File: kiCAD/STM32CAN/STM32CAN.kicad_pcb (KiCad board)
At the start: 2 copper layers, 10.2 x 20.3 mm, 6 parts, among them IC1 STM32F042G6U6, IC2 TCAN332GDCNR, Y1 7A-8.000MAAE-T

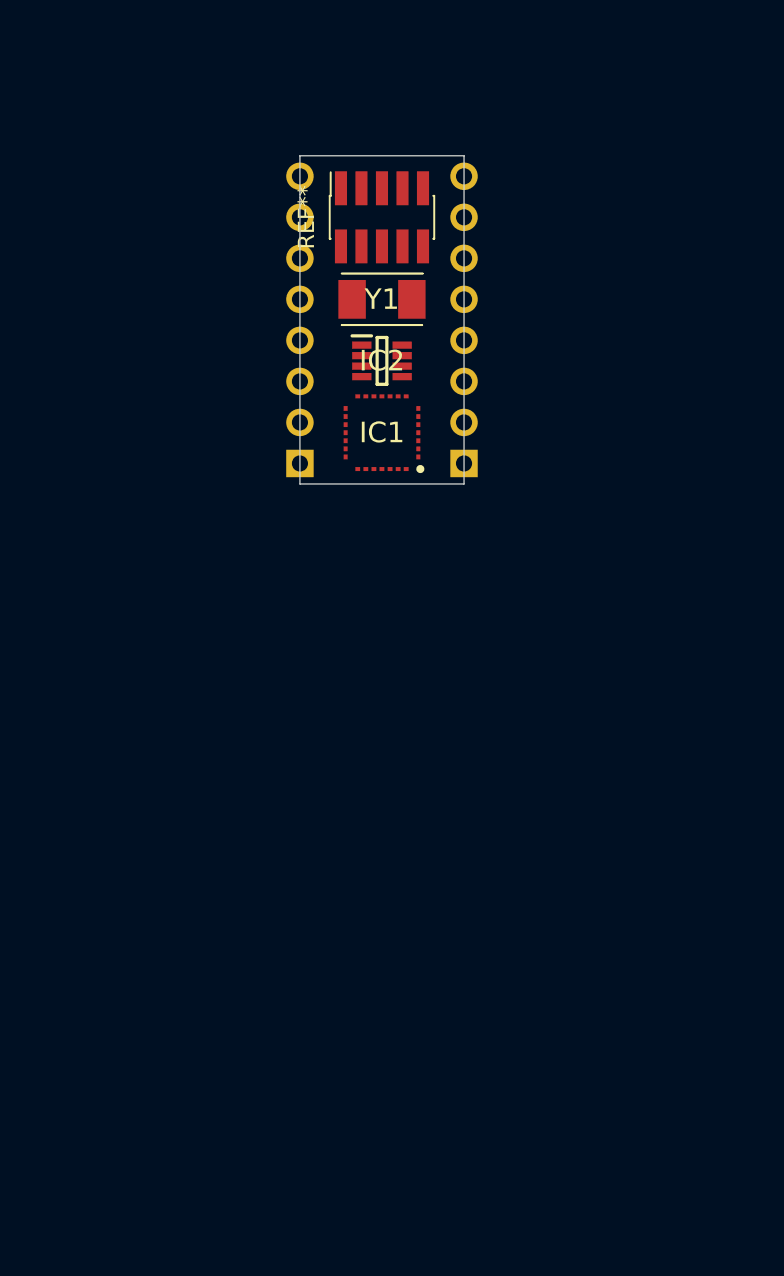
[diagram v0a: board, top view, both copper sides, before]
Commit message: Started layout
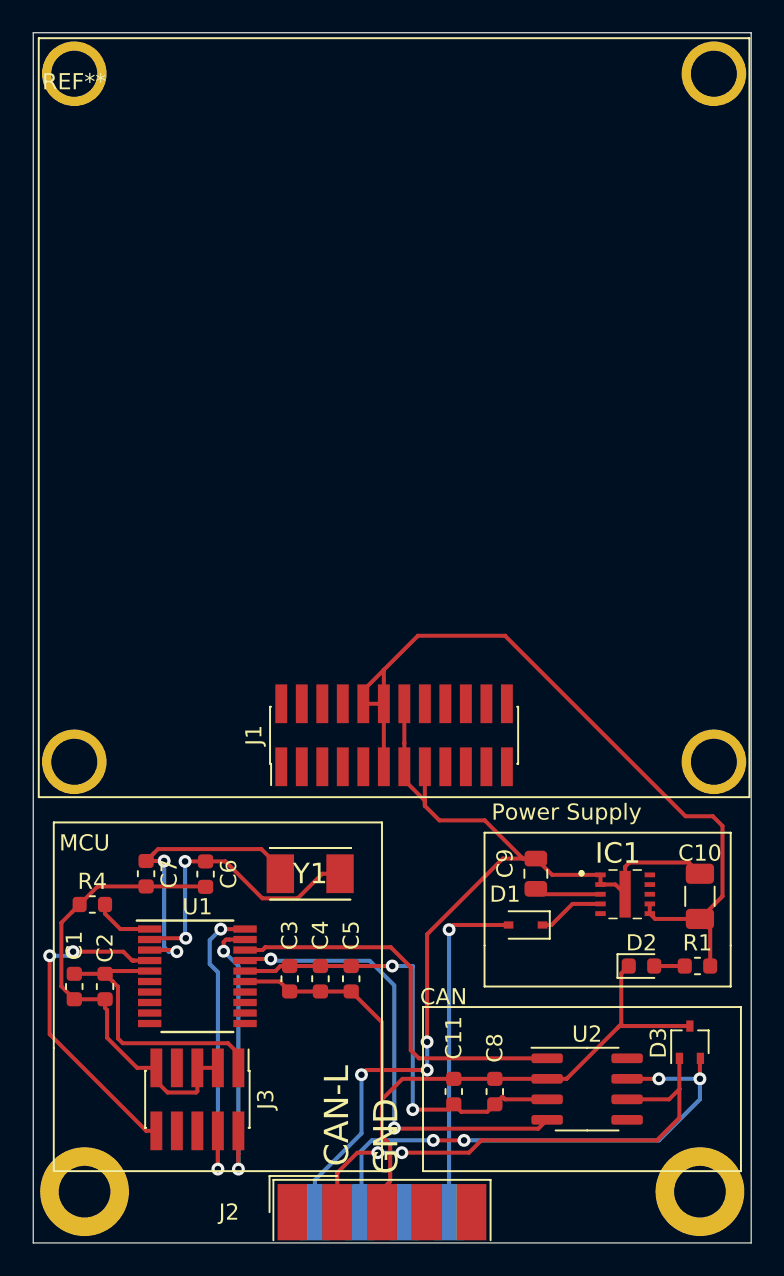
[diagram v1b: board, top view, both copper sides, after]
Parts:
- removed IC2: TCAN332GDCNR, SamacSys_Parts:SOT65P280X145-8N
- removed the REF** at (38.1, 27.9)
- removed the REF** at (33.0, 43.2)
- removed the REF** at (43.2, 43.2)
- added C1: 10nF, Capacitor_SMD:C_0603_1608Metric, F.Cu at (19.1, 75.6)
- added C10: 47uF, Capacitor_SMD:C_1206_3216Metric, F.Cu at (57.8, 70.0)
- added C11: 1uF, Capacitor_SMD:C_0603_1608Metric, F.Cu at (42.5, 82.1)
- added C2: 1uF, Capacitor_SMD:C_0603_1608Metric, F.Cu at (21.0, 75.6)
- added C3: 4.7uF, Capacitor_SMD:C_0603_1608Metric, F.Cu at (32.4, 75.1)
- added C4: 100nF, Capacitor_SMD:C_0603_1608Metric, F.Cu at (34.3, 75.1)
- added C5: 10nF, Capacitor_SMD:C_0603_1608Metric, F.Cu at (36.2, 75.1)
- added C6: 12p, Capacitor_SMD:C_0603_1608Metric, F.Cu at (27.2, 68.6)
- added C7: 12p, Capacitor_SMD:C_0603_1608Metric, F.Cu at (23.5, 68.6)
- added C8: 100nF, Capacitor_SMD:C_0603_1608Metric, F.Cu at (45.1, 82.1)
- added C9: 10uF, Capacitor_SMD:C_0805_2012Metric, F.Cu at (47.6, 68.6)
- added D1: PMEG6010CEJ, Diode_SMD:D_SOD-323, F.Cu at (47.0, 71.8)
- added D2: LED, Diode_SMD:D_0603_1608Metric, F.Cu at (54.2, 74.3)
- added D3: ESDCAN03-2BWY, Package_TO_SOT_SMD:SOT-323_SC-70, F.Cu at (57.2, 79.0)
- added J1: Conn_02x12_Odd_Even, Connector_PinHeader_1.27mm:PinHeader_2x12_P1.27mm_Vertical_SMD, F.Cu at (38.9, 60.0)
- added J2: DB9_Male, Connector_Dsub:DSUB-9_Male_EdgeMount_P2.77mm, F.Cu at (38.1, 89.5)
- added J3: Conn_02x05_Odd_Even, Connector_PinHeader_1.27mm:PinHeader_2x05_P1.27mm_Vertical_SMD, F.Cu at (26.7, 82.5)
- added Pad1: MountingHole_3.2mm_M3_ISO14580_Pad, MountingHole:MountingHole_3.2mm_M3_ISO14580_Pad, F.Cu at (19.7, 88.3)
- added Pad2: MountingHole_3.2mm_M3_ISO14580_Pad, MountingHole:MountingHole_3.2mm_M3_ISO14580_Pad, F.Cu at (57.8, 88.3)
- added R1: 470R, Resistor_SMD:R_0603_1608Metric, F.Cu at (57.6, 74.3)
- added R4: 10k, Resistor_SMD:R_0603_1608Metric, F.Cu at (20.2, 70.5)
- added REF**: ADIS-mounting, SamacSys_Parts:ADIS-mounting, F.Cu at (19.1, 19.1)
- added U1: STM32F042F6Px, Package_SO:TSSOP-20_4.4x6.5mm_P0.65mm, F.Cu at (26.7, 74.9)
- added U2: TCAN332, Package_SO:SOIC-8_3.9x4.9mm_P1.27mm, F.Cu at (50.8, 81.9)
- IC1: value STM32F042G6U6 -> LMZM23601V3; footprint SamacSys_Parts:QFN50P400X400X60-28N-D -> SamacSys_Parts:LMZM23601V5SILR
- Y1: value 7A-8.000MAAE-T -> Crystal
- moved Y1 35.8 mm to (33.7, 68.6)
- moved IC1 32.1 mm to (52.7, 69.8), turned to 0 degrees
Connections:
- IC1 pad 1: Net-(IC1-Pad1) -> GNDREF
- IC1 pad 11: Net-(IC1-Pad11) -> GNDREF
- IC1 pad 2: Net-(IC1-Pad2) -> GNDREF
- IC1 pad 3: Net-(IC1-Pad3) -> Net-(C9-Pad1)
- IC1 pad 4: Net-(IC1-Pad4) -> Net-(C9-Pad1)
- IC1 pad 6: Net-(IC1-Pad6) -> +3V3
- IC1 pad 7: Net-(IC1-Pad7) -> +3V3
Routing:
- net GNDREF: track 0.00 -> 137.7 mm, vias 0 -> 3
- net +3V3: track 0.00 -> 96.3 mm, vias 0 -> 2
- net Net-(D3-Pad2): track 0.00 -> 33.2 mm, vias 0 -> 4
- net Net-(D3-Pad1): track 0.00 -> 32.7 mm, vias 0 -> 2
- net /CAN_RXD: track 0.00 -> 28.5 mm, vias 0 -> 2
- net /CAN_TXD: track 0.00 -> 24.6 mm
- net /POWER_IN: track 0.00 -> 21.3 mm, vias 0 -> 1
- net /~RESET: track 0.00 -> 20.5 mm, vias 0 -> 2
- net /SWCLK: track 0.00 -> 19.2 mm, vias 0 -> 2
- net Net-(C7-Pad1): track 0.00 -> 18.5 mm, vias 0 -> 2
- net Net-(C6-Pad1): track 0.00 -> 18.3 mm, vias 0 -> 2
- net /SDWIO: track 0.00 -> 18.2 mm, vias 0 -> 2
- net Net-(C9-Pad1): track 0.00 -> 8.27 mm
- net Net-(R4-Pad2): track 0.00 -> 3.73 mm
- net Net-(D2-Pad2): track 0.00 -> 1.89 mm
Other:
- board size 10.2 x 20.3 mm -> 44.5 x 74.9 mm
- board text added: "CAN"
- board text added: "CAN-H"
- board text added: "CAN-L"
- board text added: "GND"
- board text added: "MCU"
- board text added: "PWR"
- board text added: "Power Supply"

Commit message: Rev.- complete. Board ordered
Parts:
- added GG1: LOGO, SamacSys_Parts:sign-small-Cu, B.Cu at (39.4, 45.7)
- added GG2: LOGO, SamacSys_Parts:sign-small, F.Cu at (38.1, 45.7)
- added QR1: QR_CANtest, SamacSys_Parts:QR_CANtest, B.Cu at (38.9, 31.8)
- added QR2: QR_CANtest, SamacSys_Parts:QR_CANtest, F.Cu at (38.9, 31.8)
- J1: footprint Connector_PinHeader_1.27mm:PinHeader_2x12_P1.27mm_Vertical_SMD -> Connector_PinSocket_1.27mm:PinSocket_2x12_P1.27mm_Vertical_SMD
- turned J1 to 270 degrees
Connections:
- Pad1 pad GNDREF: (no net) -> GNDREF
- Pad2 pad GNDREF: (no net) -> GNDREF
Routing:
- net /SPI_MOSI: track 0.00 -> 65.7 mm, vias 0 -> 2
- net /MCU_IO3: track 0.00 -> 52.0 mm, vias 0 -> 2
- net /MCU_IO2: track 0.00 -> 43.5 mm, vias 0 -> 2
- net /MCU_IO0: track 0.00 -> 42.1 mm, vias 0 -> 2
- net /SPI_NSS: track 0.00 -> 37.9 mm, vias 0 -> 2
- net /MCU_IO4: track 0.00 -> 35.4 mm, vias 0 -> 2
- net /SPI_SCK: track 0.00 -> 31.0 mm, vias 0 -> 2
- net /SPI_MISO: track 0.00 -> 26.7 mm, vias 0 -> 2
- net /MCU_IO1: track 0.00 -> 24.7 mm, vias 0 -> 2
- net +3V3: track 96.3 -> 117.0 mm, vias 2 -> 4
- net GNDREF: track 137.7 -> 144.6 mm, vias 3 -> 2
- net /SDWIO: track 18.2 -> 15.4 mm
- net Net-(C7-Pad1): track 18.5 -> 21.1 mm
- net Net-(C6-Pad1): track 18.3 -> 17.1 mm, vias 2 -> 0
- net Net-(J1-Pad16): track 0.00 -> 0.98 mm
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- added copper zone on B.Cu, net GNDREF
- added copper zone on F.Cu, net GNDREF
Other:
- board text added: "SWD"
